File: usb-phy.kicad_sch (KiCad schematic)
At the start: 105 parts, among them J12 614004184726, J13 USB4105-GF-A, J14 USB4105-GF-A, Q17 BSS138PW, U15 TPS7B8133DRVR, U16 TPD4E05U06QDQARQ1, U17 TPD4E05U06QDQARQ1, U18 SN74HC595D, U19 MAX3421EETJ+, U20 FT4232H-56Q, U21 TPD4E05U06QDQARQ1, U22 TXU0304BQAR, U23 TXU0304BQAR, U24 TXU0304BQAR, U25 TUSB1106RSVR, Y1 ABM8G-12.000MHZ-18-D2Y-T, Y2 ABM8G-12.000MHZ-18-D2Y-T

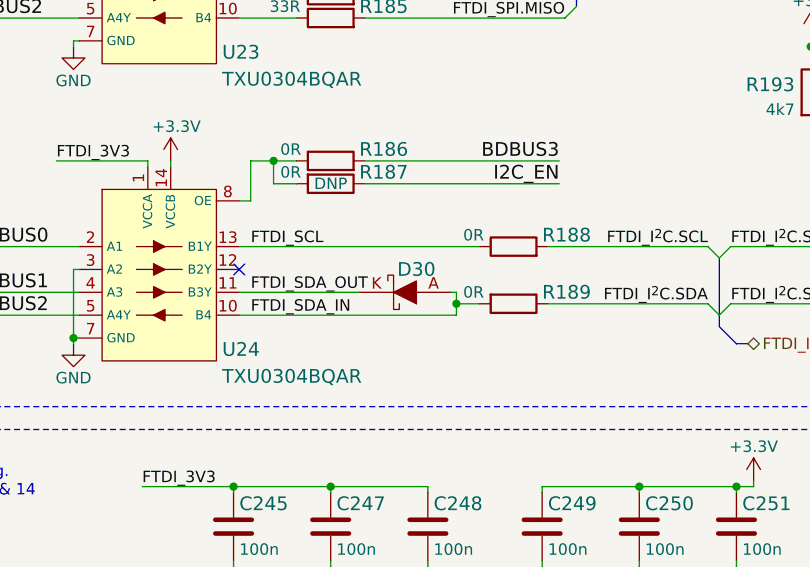
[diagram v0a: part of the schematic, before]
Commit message: Fix libraries, sync schematic with PCB
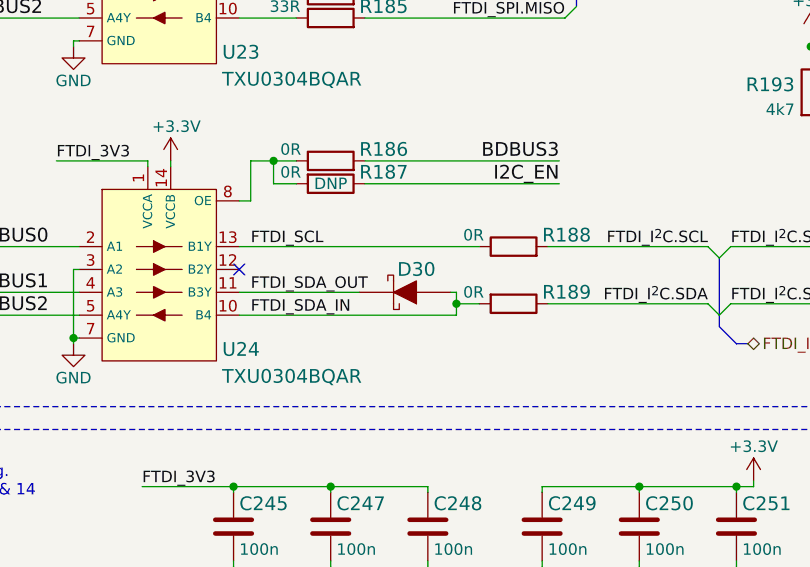
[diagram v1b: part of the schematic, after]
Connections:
- net FTDI_SDA_IN: now also D30.2; no longer D30.A
- net FTDI_SDA_OUT: now also D30.1; no longer D30.K
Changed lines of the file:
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@@
       (effects (font (size 1.524 1.524)) (justify left) hide)
     )
-    (pin "A")
-    (pin "K")
+    (pin "1")
+    (pin "2")
   )
   (symbol (lib_id "antmicroResistors0402:R_33R_0402") (at 97.79 44.45 0) (unit 1)

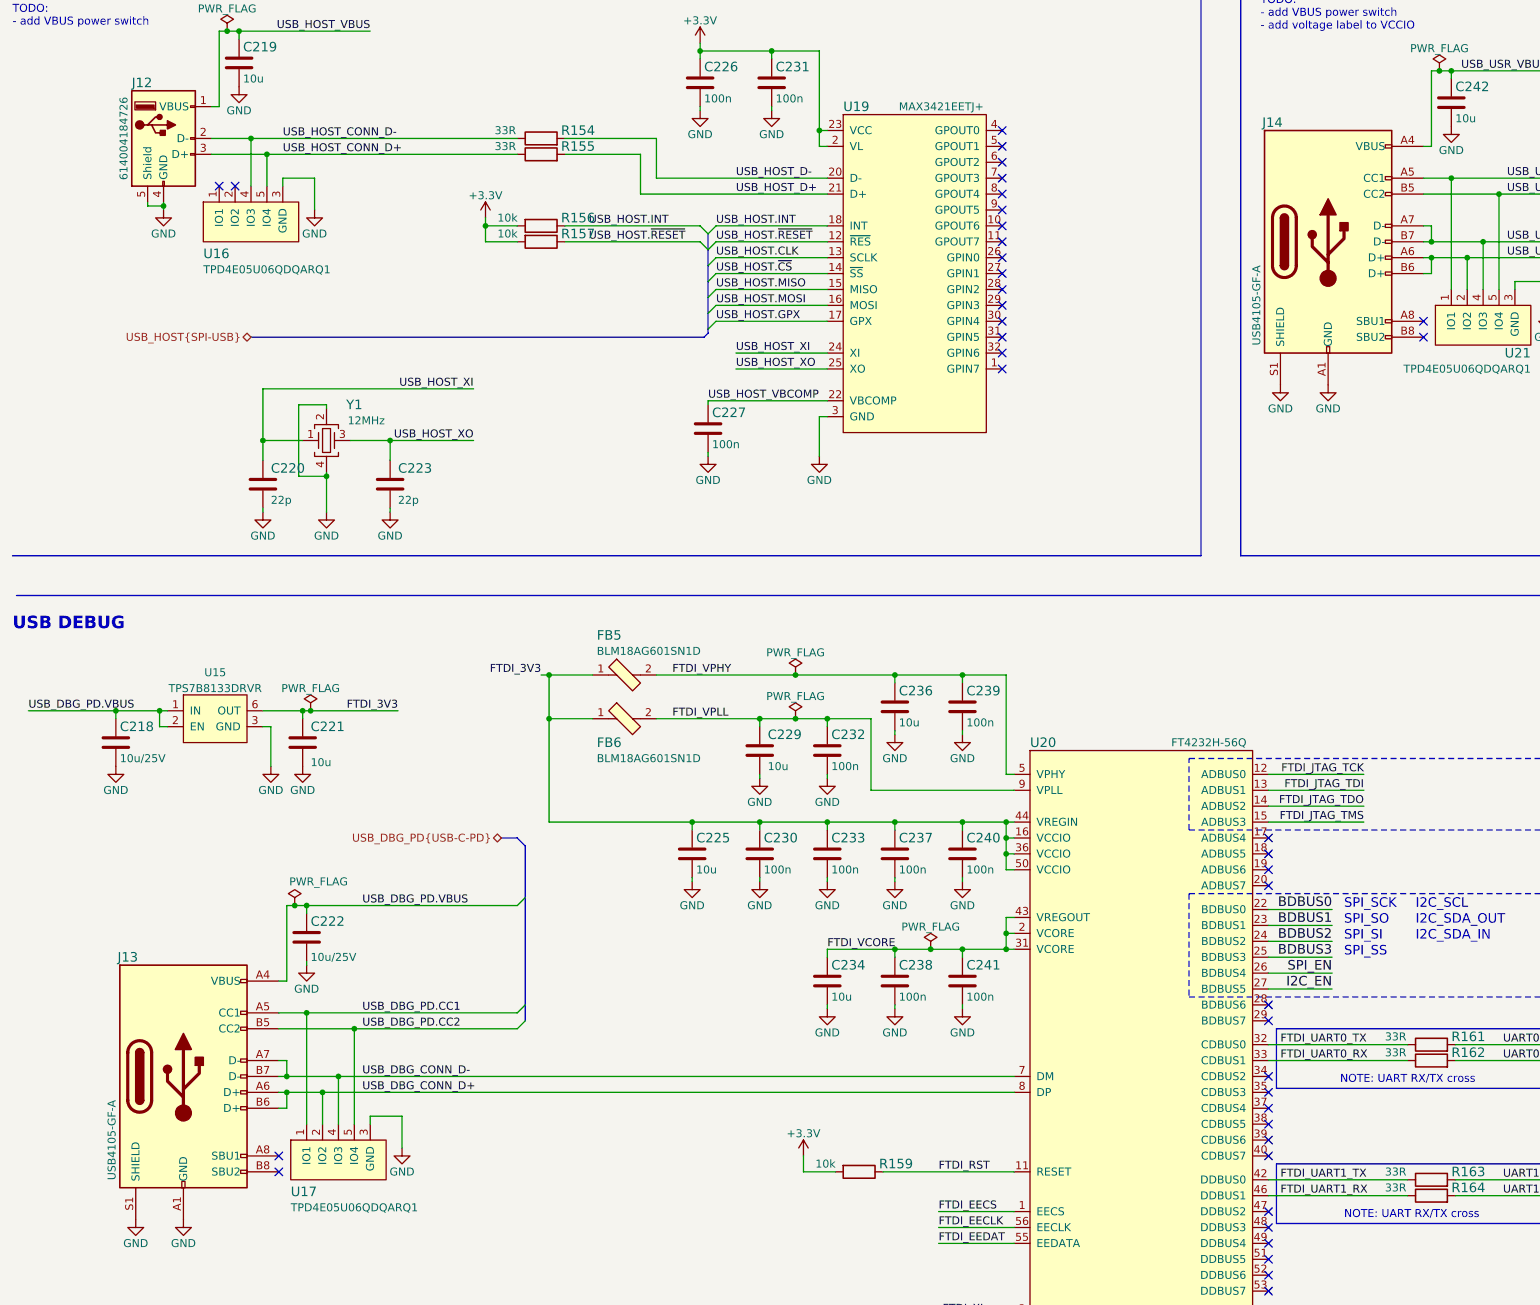
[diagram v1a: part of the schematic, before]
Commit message: Replace USB-C connectors with vertical ones
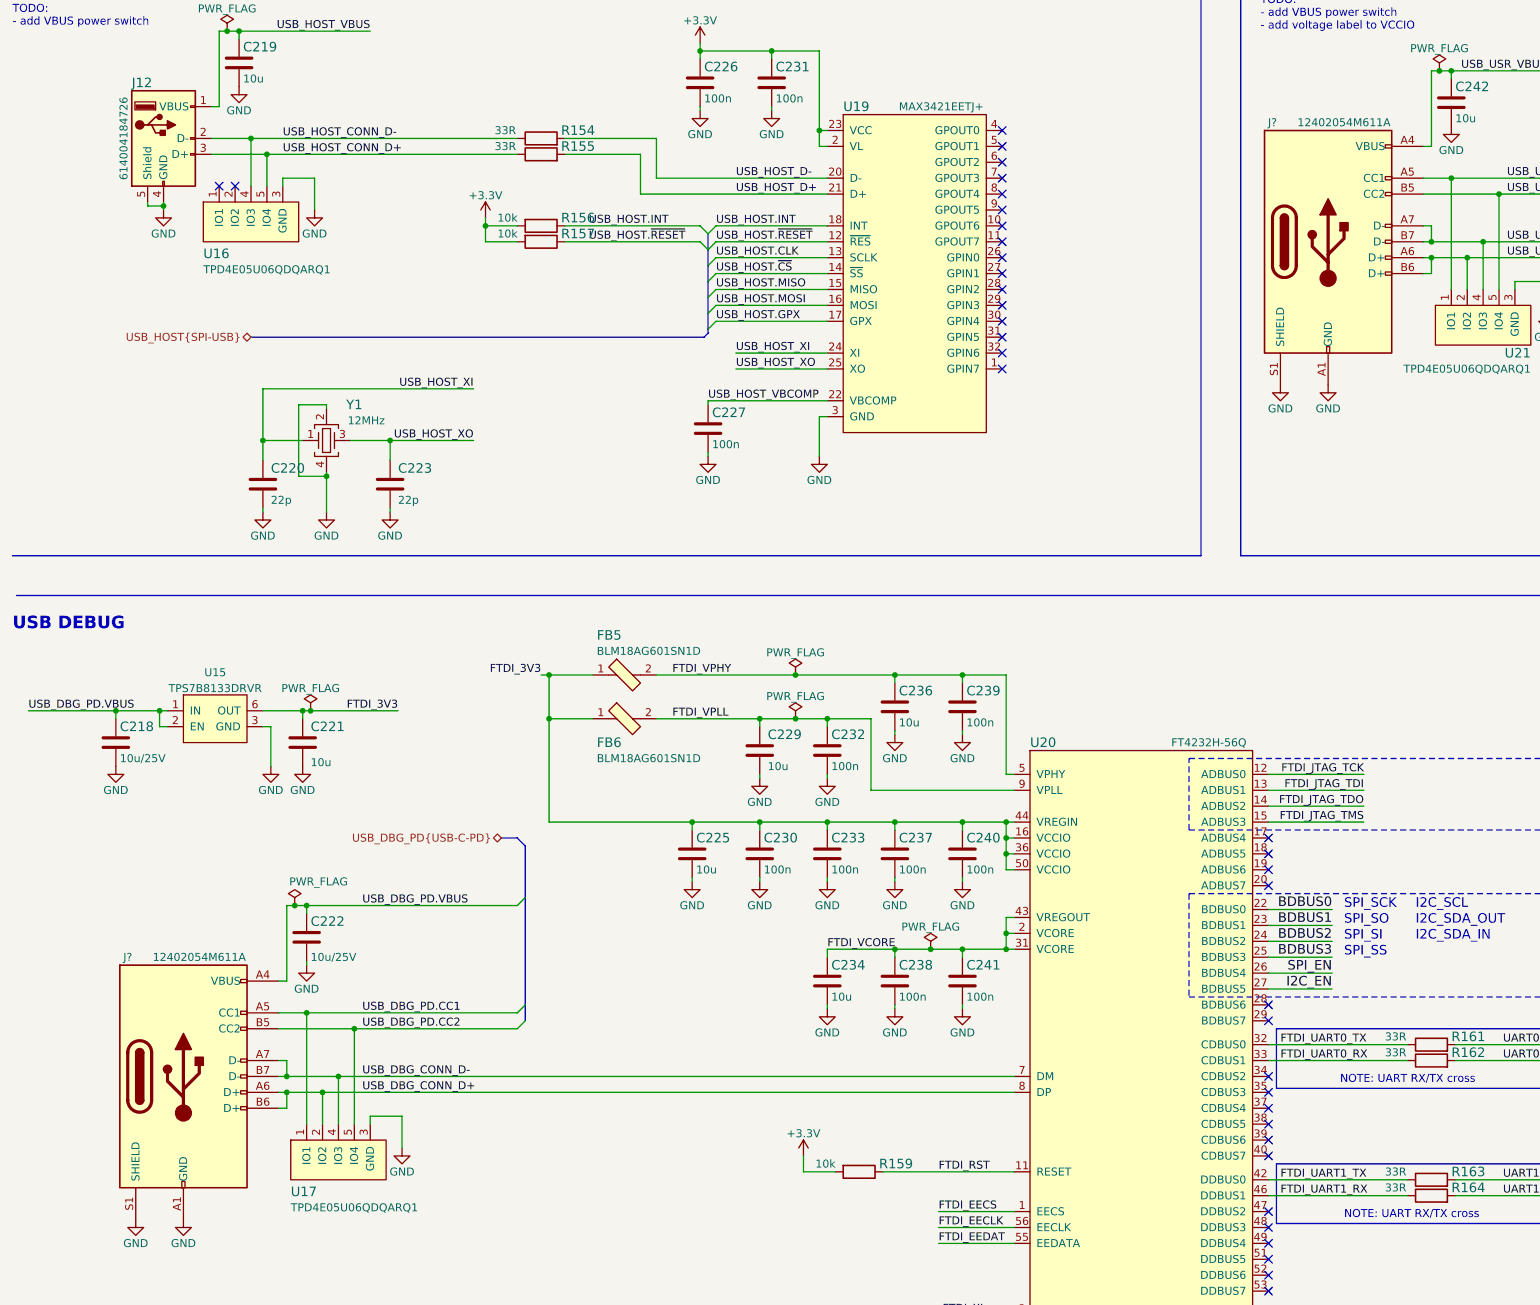
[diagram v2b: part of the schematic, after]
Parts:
- removed J13, J14: USB4105-GF-A, antmicro-footprints:GCT_USB4105-GF-A, symbol antmicroUSBDVIHDMIConnectors:USB4105-GF-A
- added J? (x2): 12402054M611A, antmicro-footprints:12402054M611A, symbol antmicroUSBDVIHDMIConnectors:12402054M611A
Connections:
- net GND: now also J?.A1 (GND), J?.A1 (GND), J?.A12 (GND), J?.A12 (GND), J?.B1 (GND), J?.B1 (GND), J?.B12 (GND), J?.B12 (GND), J?.S1 (SHIELD), J?.S1 (SHIELD)
- net USB_DBG_CONN_D+: now also J?.A6 (D+), J?.B6 (D+)
- net USB_DBG_CONN_D-: now also J?.A7 (D-), J?.B7 (D-)
- net USB_DBG_PD.CC1: now also J?.A5 (CC1)
- net USB_DBG_PD.CC2: now also J?.B5 (CC2)
- net USB_DBG_PD.VBUS: now also J?.A4 (VBUS), J?.A9 (VBUS), J?.B4 (VBUS), J?.B9 (VBUS)
- net USB_USR_CC1: now also J?.A5 (CC1)
- net USB_USR_CC2: now also J?.B5 (CC2)
- net USB_USR_CONN_D+: now also J?.A6 (D+), J?.B6 (D+)
- net USB_USR_CONN_D-: now also J?.A7 (D-), J?.B7 (D-)
- net USB_USR_VBUS: now also J?.A4 (VBUS), J?.A9 (VBUS), J?.B4 (VBUS), J?.B9 (VBUS)
- no-connect marks 47 -> 43
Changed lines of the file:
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@@
   (no_connect (at 171.45 48.26))
   (no_connect (at 213.995 158.75))
-  (no_connect (at 55.88 207.01))
   (no_connect (at 171.45 76.2))
   (no_connect (at 171.45 55.88))
@@
   (no_connect (at 171.45 43.18))
   (no_connect (at 213.995 201.93))
-  (no_connect (at 238.76 73.66))
-  (no_connect (at 55.88 204.47))
   (no_connect (at 171.45 40.64))
-  (no_connect (at 238.76 71.12))
   (no_connect (at 171.45 45.72))
   (no_connect (at 213.995 218.44))
@@
     (pin "2")
   )
+  (symbol (lib_id "antmicroUSBDVIHDMIConnectors:12402054M611A") (at 40.64 191.77 0) (unit 1)
+    (in_bom yes) (on_board yes)
+    (property "Reference" "J?" (id 0) (at 31.75 172.72 0))
+    (property "Value" "12402054M611A" (id 1) (at 43.18 172.72 0))
+    (property "Footprint" "antmicro-footprints:12402054M611A" (id 2) (at 24.13 172.72 0)
+      (effects (font (size 1.27 1.27)) (justify left bottom) hide)
+    )
+    (property "Datasheet" "https://cdn.amphenol-cs.com/media/wysiwyg/files/drawing/12402054-3.pdf" (id 3) (at 40.64 191.77 0)
+      (effects (font (size 1.27 1.27)) (justify left bottom) hide)
+    )
+    (property "Manufacturer" "Amphenol" (id 4) (at 24.13 171.45 0)
+      (effects (font (size 1.27 1.27)) (justify left bottom) hide)
+    )
+    (property "MPN" "12402054M611A" (id 5) (at 31.75 168.91 0)
+      (effects (font (size 1.27 1.27)) hide)
+    )
+    (pin "A1")
+    (pin "A12")
+    (pin "A4")
+    (pin "A5")
+    (pin "A6")
+    (pin "A7")
+    (pin "A9")
+    (pin "B1")
+    (pin "B12")
+    (pin "B4")
+    (pin "B5")
+    (pin "B6")
+    (pin "B7")
+    (pin "B9")
+    (pin "S1")
+  )
   (symbol (lib_id "power:GND") (at 165.1 137.16 0) (mirror y) (unit 1)
     (in_bom yes) (on_board yes)
@@
     (pin "2")
   )
-  (symbol (lib_id "antmicroUSBDVIHDMIConnectors:USB4105-GF-A") (at 223.52 58.42 0) (unit 1)
-    (in_bom yes) (on_board yes)
-    (property "Reference" "J14" (id 0) (at 214.63 39.37 0)
-      (effects (font (size 1.524 1.524)))
-    )
-    (property "Value" "USB4105-GF-A" (id 1) (at 212.09 68.58 90))
-    (property "Footprint" "antmicro-footprints:GCT_USB4105-GF-A" (id 2) (at 207.01 39.37 0)
-      (effects (font (size 1.27 1.27)) (justify left bottom) hide)
-    )
-    (property "Datasheet" "https://gct.co/files/drawings/usb4105.pdf" (id 3) (at 223.52 58.42 0)
-      (effects (font (size 1.27 1.27)) (justify left bottom) hide)
-    )
-    (property "Manufacturer" "GCT" (id 4) (at 207.01 38.1 0)
-      (effects (font (size 1.27 1.27)) (justify left bottom) hide)
-    )
-    (property "MPN" "USB4105-GF-A" (id 5) (at 214.63 35.56 0)
-      (effects (font (size 1.27 1.27)) hide)
-    )
-    (pin "A1")
-    (pin "A12")
-    (pin "A4")
-    (pin "A5")
-    (pin "A6")
-    (pin "A7")
-    (pin "A8")
-    (pin "A9")
-    (pin "B1")
-    (pin "B12")
-    (pin "B4")
-    (pin "B5")
-    (pin "B6")
-    (pin "B7")
-    (pin "B8")
-    (pin "B9")
-    (pin "S1")
-  )
   (symbol (lib_id "power:GND") (at 60.325 173.99 0) (unit 1)
     (in_bom yes) (on_board yes)
@@
     (pin "2")
   )
-  (symbol (lib_id "antmicroUSBDVIHDMIConnectors:USB4105-GF-A") (at 40.64 191.77 0) (unit 1)
-    (in_bom yes) (on_board yes)
-    (property "Reference" "J13" (id 0) (at 31.75 172.72 0)
-      (effects (font (size 1.524 1.524)))
-    )
-    (property "Value" "USB4105-GF-A" (id 1) (at 29.21 201.93 90))
-    (property "Footprint" "antmicro-footprints:GCT_USB4105-GF-A" (id 2) (at 24.13 172.72 0)
-      (effects (font (size 1.27 1.27)) (justify left bottom) hide)
-    )
-    (property "Datasheet" "https://gct.co/files/drawings/usb4105.pdf" (id 3) (at 40.64 191.77 0)
-      (effects (font (size 1.27 1.27)) (justify left bottom) hide)
-    )
-    (property "Manufacturer" "GCT" (id 4) (at 24.13 171.45 0)
-      (effects (font (size 1.27 1.27)) (justify left bottom) hide)
-    )
-    (property "MPN" "USB4105-GF-A" (id 5) (at 31.75 168.91 0)
-      (effects (font (size 1.27 1.27)) hide)
-    )
-    (pin "A1")
-    (pin "A12")
-    (pin "A4")
-    (pin "A5")
-    (pin "A6")
-    (pin "A7")
-    (pin "A8")
-    (pin "A9")
-    (pin "B1")
-    (pin "B12")
-    (pin "B4")
-    (pin "B5")
-    (pin "B6")
-    (pin "B7")
-    (pin "B8")
-    (pin "B9")
-    (pin "S1")
-  )
   (symbol (lib_id "antmicroCapacitorsmisc:C_100n_0201") (at 352.425 241.935 0) (unit 1)
     (in_bom yes) (on_board yes)
@@
     (pin "2")
   )
+  (symbol (lib_id "antmicroUSBDVIHDMIConnectors:12402054M611A") (at 223.52 58.42 0) (unit 1)
+    (in_bom yes) (on_board yes)
+    (property "Reference" "J?" (id 0) (at 214.63 39.37 0))
+    (property "Value" "12402054M611A" (id 1) (at 226.06 39.37 0))
+    (property "Footprint" "antmicro-footprints:12402054M611A" (id 2) (at 207.01 39.37 0)
+      (effects (font (size 1.27 1.27)) (justify left bottom) hide)
+    )
+    (property "Datasheet" "https://cdn.amphenol-cs.com/media/wysiwyg/files/drawing/12402054-3.pdf" (id 3) (at 223.52 58.42 0)
+      (effects (font (size 1.27 1.27)) (justify left bottom) hide)
+    )
+    (property "Manufacturer" "Amphenol" (id 4) (at 207.01 38.1 0)
+      (effects (font (size 1.27 1.27)) (justify left bottom) hide)
+    )
+    (property "MPN" "12402054M611A" (id 5) (at 214.63 35.56 0)
+      (effects (font (size 1.27 1.27)) hide)
+    )
+    (pin "A1")
+    (pin "A12")
+    (pin "A4")
+    (pin "A5")
+    (pin "A6")
+    (pin "A7")
+    (pin "A9")
+    (pin "B1")
+    (pin "B12")
+    (pin "B4")
+    (pin "B5")
+    (pin "B6")
+    (pin "B7")
+    (pin "B9")
+    (pin "S1")
+  )
   (symbol (lib_id "antmicroResistors0402:R_33R_0402") (at 341.63 140.97 0) (unit 1)
